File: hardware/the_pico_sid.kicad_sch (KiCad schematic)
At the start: 16 parts, among them J1 SWD, U1 TL084, U2 SID_6581, U3 Pico, U4 4050, U5 4050, U6 74HC245

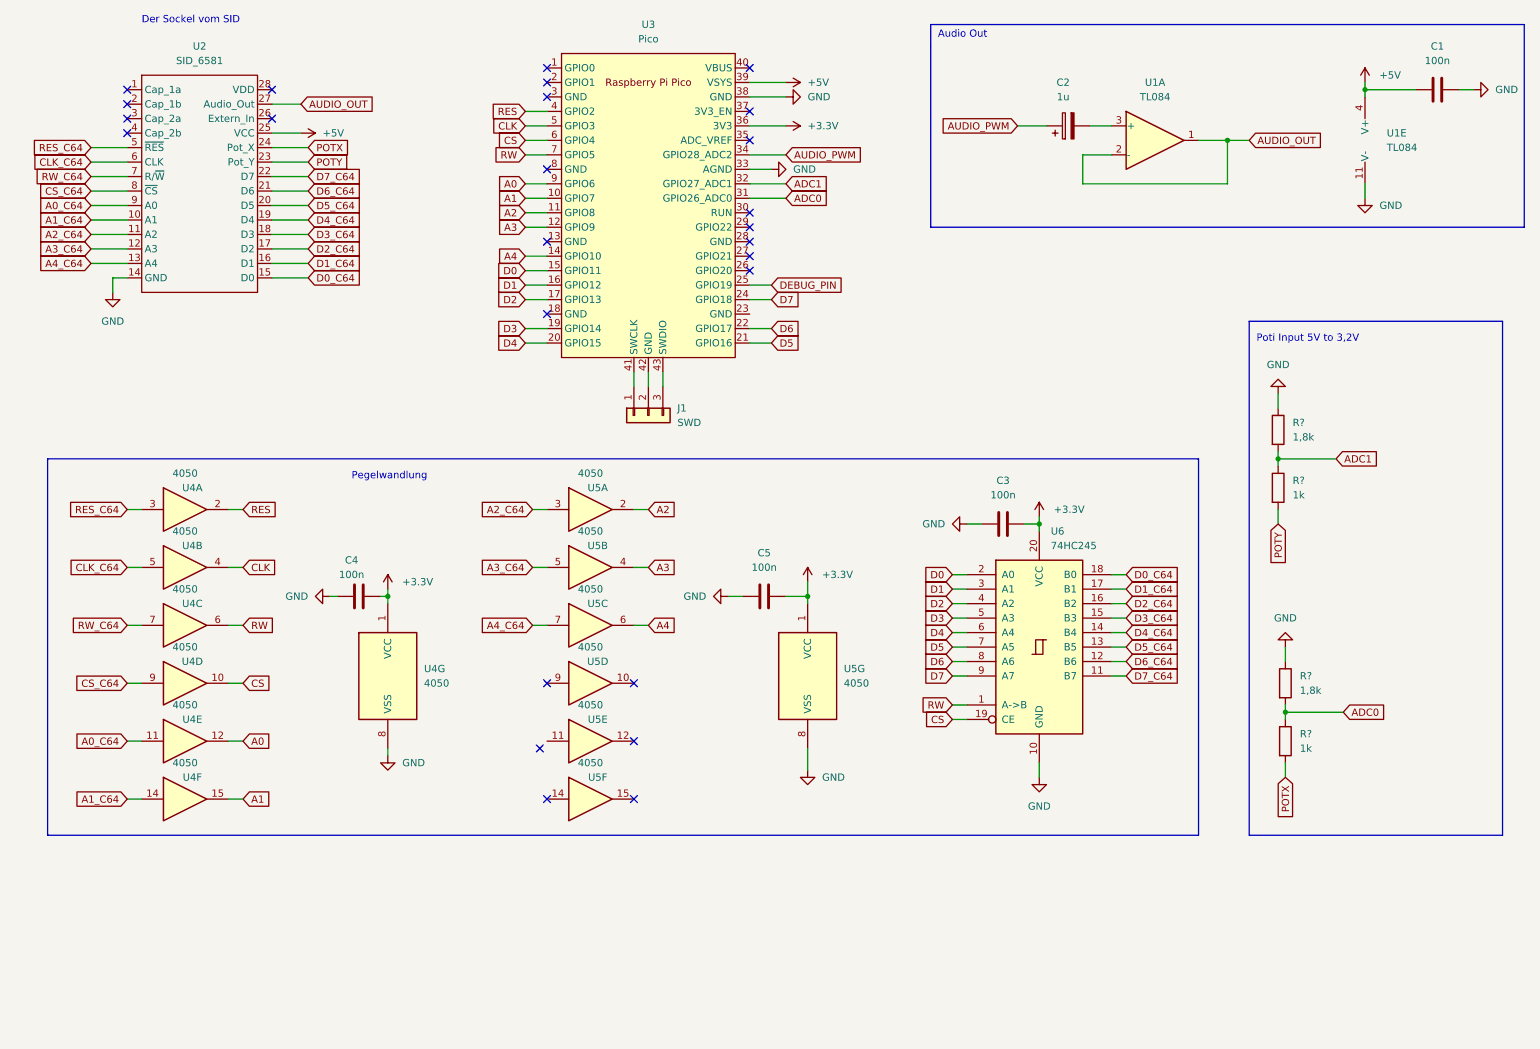
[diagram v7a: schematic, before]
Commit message: schematic: change tl084 with lm324. added potx, poty support
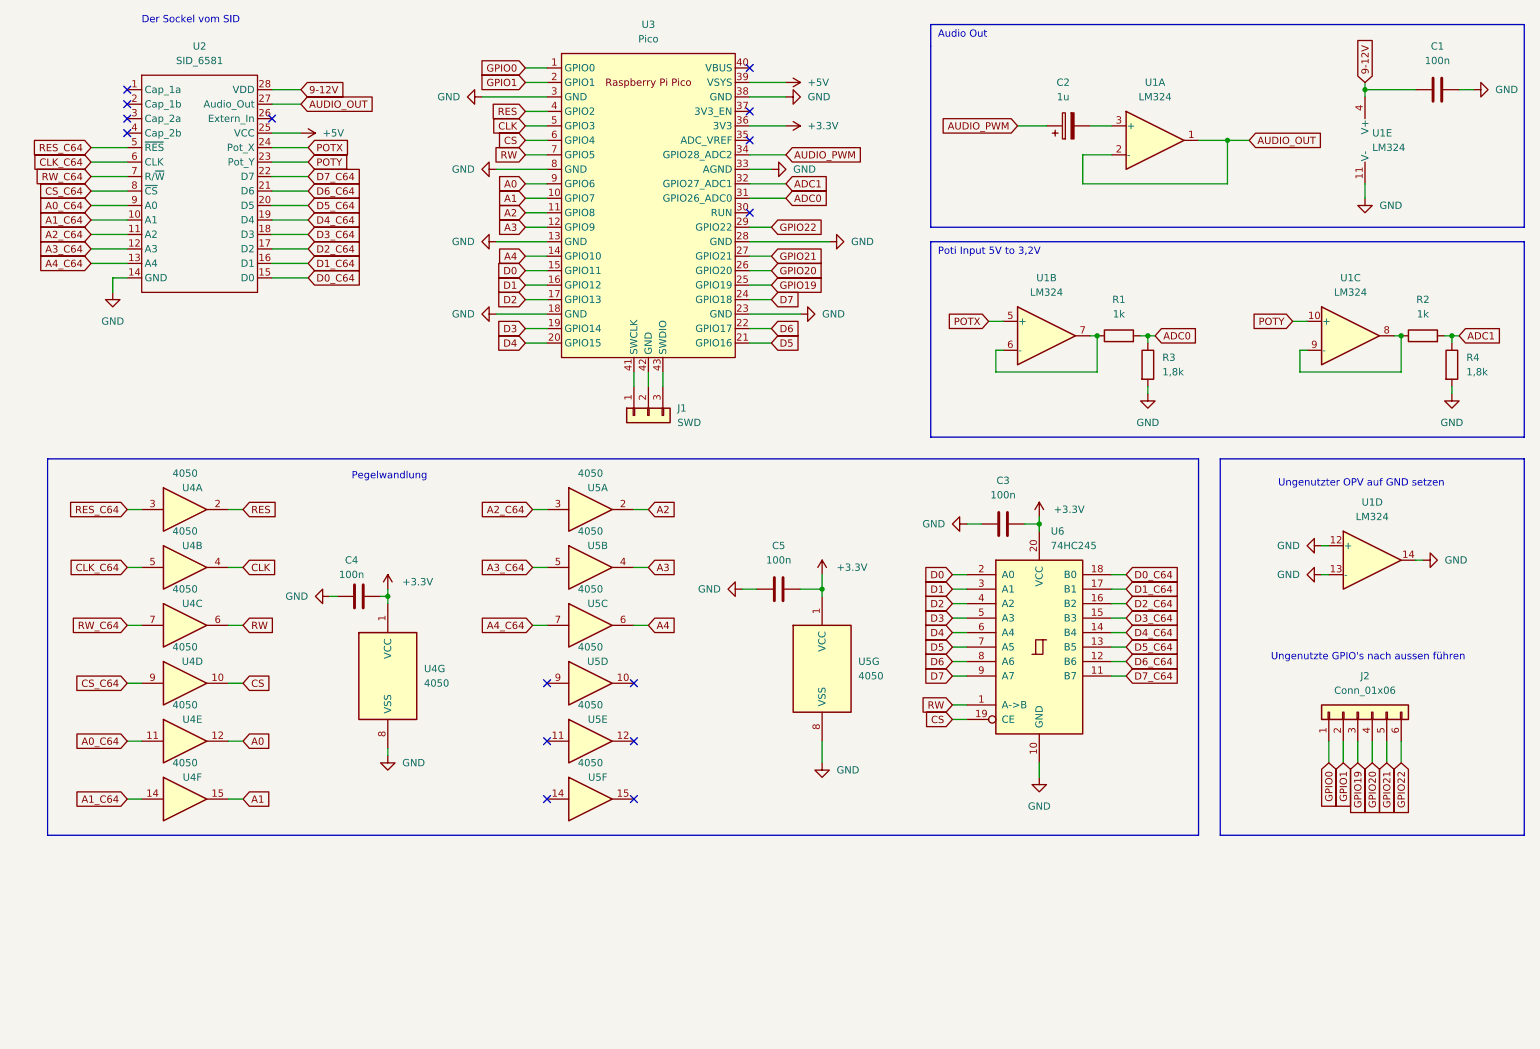
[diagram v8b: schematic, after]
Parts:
- removed U1: TL084, symbol Amplifier_Operational:TL084
- added J2: Conn_01x06, symbol Connector_Generic:Conn_01x06
- added U1: LM324, symbol Amplifier_Operational:LM324
- gave numbers to parts that had none: 4
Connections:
- net +5V: no longer C1.1
- net ADC0: now also R1.2, R3.1; no longer R1.1, R3.2
- net ADC1: now also R2.2, R4.1; no longer R2.1, R4.2
- net AUDIO_OUT: now also U1.1, U1.2 (-)
- net GND: now also R3.2, R4.2, U3.13 (GND), U3.18 (GND), U3.23 (GND), U3.28 (GND), U3.3 (GND), U3.8 (GND), U1.11 (V-), U1.12 (+), U1.13 (-), U1.14; no longer R3.1, R4.1
- net POTX: now also U1.5 (+); no longer R1.2
- net POTY: now also U1.10 (+); no longer R2.2
- net at C2.2: now also U1.3 (+)
- net GPIO0: now reaches U3.1 (GPIO0)
- net GPIO0: now also J2.1 (Pin_1)
- net GPIO1: now reaches U3.2 (GPIO1)
- net GPIO1: now also J2.2 (Pin_2)
- net GPIO20: now reaches U3.26 (GPIO20)
- net GPIO20: now also J2.4 (Pin_4)
- net GPIO21: now reaches U3.27 (GPIO21)
- net GPIO21: now also J2.5 (Pin_5)
- net GPIO22: now reaches U3.29 (GPIO22)
- net GPIO22: now also J2.6 (Pin_6)
- net 9-12V: now reaches U2.28 (VDD)
- net 9-12V: now also C1.1, U1.4 (V+)
- net DEBUG_PIN renamed GPIO19
- net GPIO19: now also J2.3 (Pin_3)
- new net: R1.1, U1.6 (-), U1.7
- new net: R2.1, U1.8, U1.9 (-)
- no-connect marks 26 -> 15
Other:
- note added: "Ungenutzte GPIO's nach aussen führen"
- note added: "Ungenutzter OPV auf GND setzen"
- moved on the sheet: C5, R1, R2, R3, R4, U5G
